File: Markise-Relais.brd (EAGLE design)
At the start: 160 x 100 mm, 13 parts, among them K1 FINDER-43.41, K2 FINDER-43.41

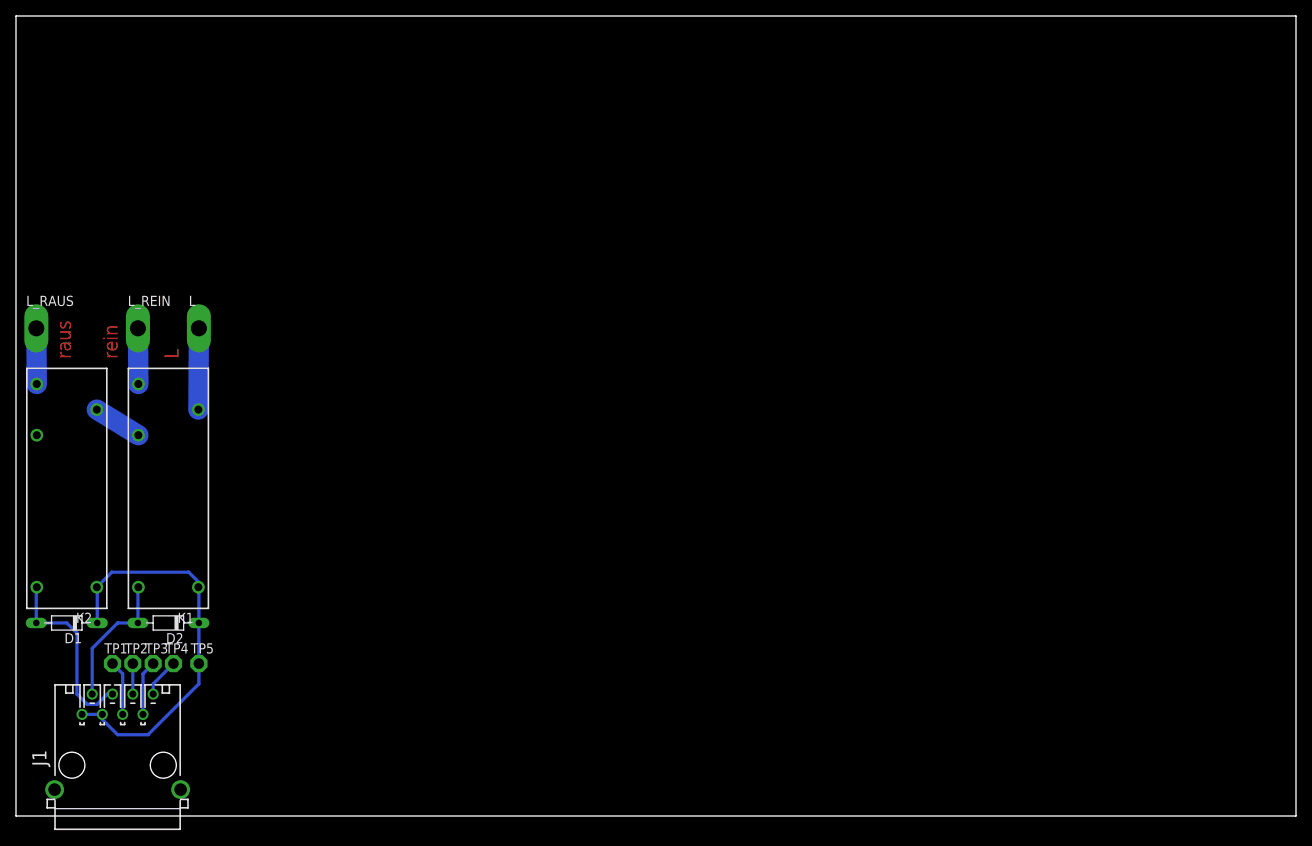
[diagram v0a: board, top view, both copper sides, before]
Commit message: Readme und Lizenz aktualisiert, Schaltpläne optimiert
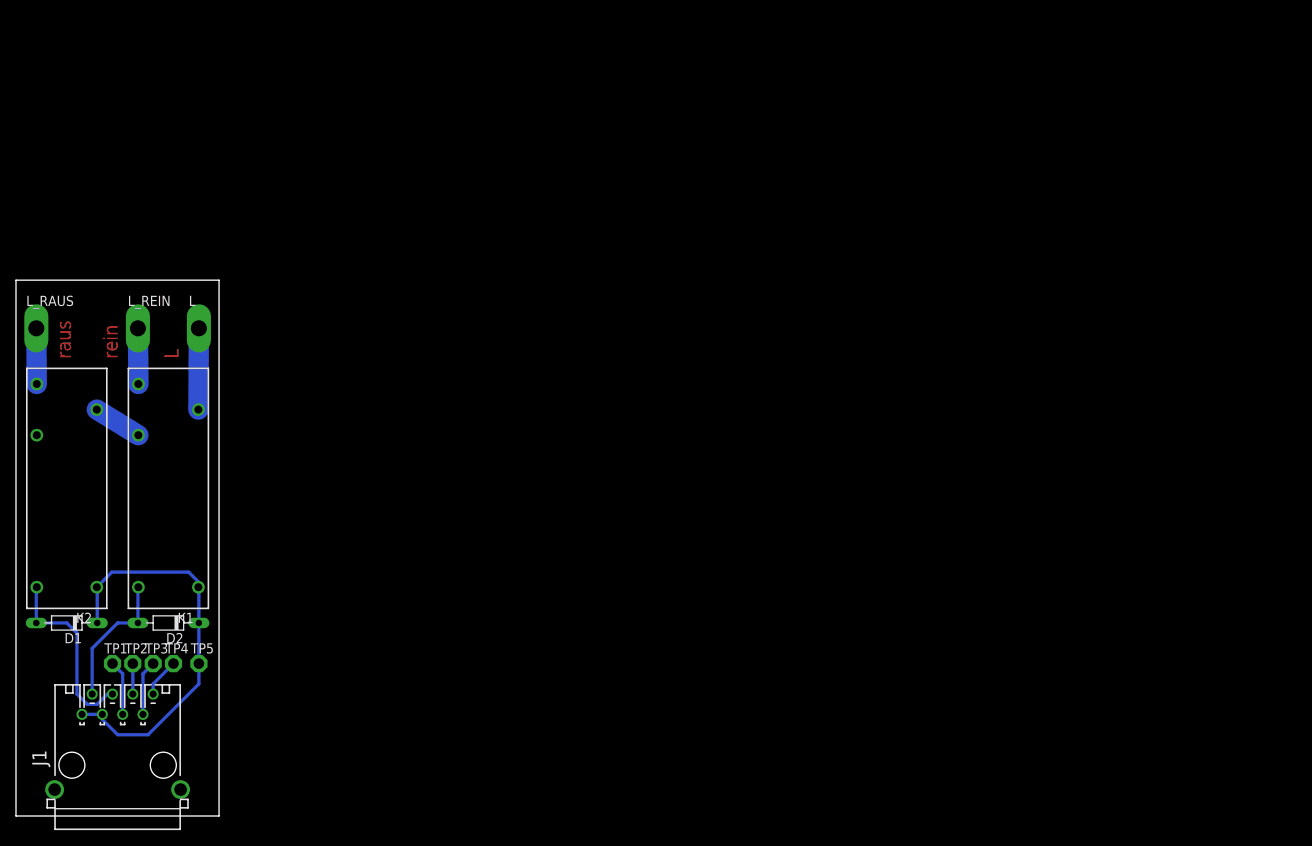
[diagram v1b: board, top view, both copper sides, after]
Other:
- board size 160 x 100 mm -> 25.4 x 67 mm
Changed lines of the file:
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@@
 <board>
 <plain>
-<wire x1="0" y1="0" x2="160" y2="0" width="0" layer="20"/>
-<wire x1="160" y1="0" x2="160" y2="100" width="0" layer="20"/>
-<wire x1="160" y1="100" x2="0" y2="100" width="0" layer="20"/>
-<wire x1="0" y1="100" x2="0" y2="0" width="0" layer="20"/>
+<wire x1="0" y1="0" x2="25.38" y2="0" width="0" layer="20"/>
+<wire x1="25.38" y1="0" x2="25.38" y2="66.98" width="0" layer="20"/>
+<wire x1="25.38" y1="66.98" x2="0" y2="66.98" width="0" layer="20"/>
+<wire x1="0" y1="66.98" x2="0" y2="0" width="0" layer="20"/>
 <text x="5.08" y="57.15" size="1.778" layer="1" font="vector" ratio="15" rot="R90" align="top-left">raus</text>
 <text x="12.7" y="57.15" size="1.778" layer="1" font="vector" ratio="15" rot="R90">rein</text>
